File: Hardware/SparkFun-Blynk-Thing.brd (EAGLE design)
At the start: 50 x 41.9 mm, 103 parts, among them IC1 LMV358, Q1 2.5A/30V, Q2 MMBT2222A, Q3 MMBT2222A, U1 MCP73831, U2 ESP8266, U3 AP2112K-3.3V, U4 FT231XS-U, U5 W25Q32FVSS, U6 SI7021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

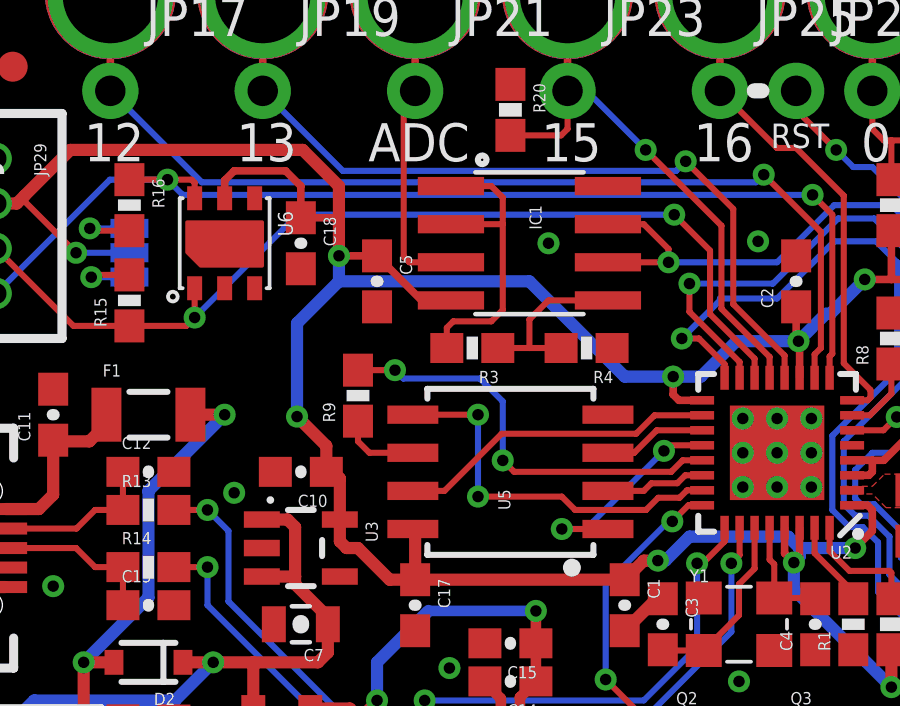
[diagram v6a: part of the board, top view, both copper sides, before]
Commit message: Fixing Op amp power supply.
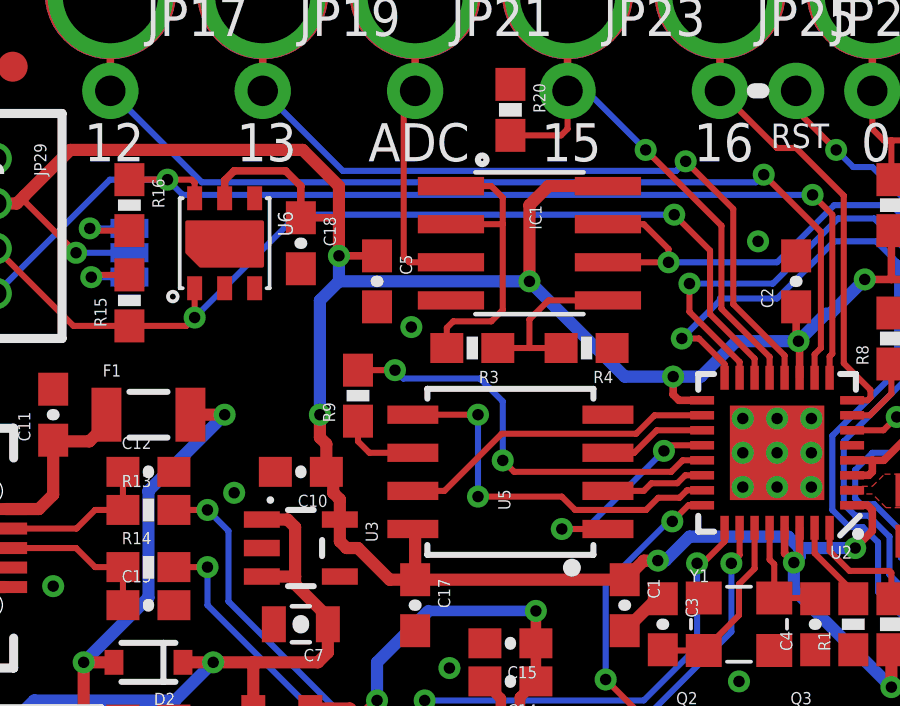
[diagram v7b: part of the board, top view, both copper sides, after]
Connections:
- net GND: now also IC1.4; no longer IC1.8
- net VCC: now also IC1.8; no longer IC1.4
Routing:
- net VCC: track 159.2 -> 160.8 mm, vias 11 -> 12
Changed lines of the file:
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@@
 <contactref element="D4" pad="1"/>
 <contactref element="C9" pad="1"/>
-<contactref element="IC1" pad="4"/>
 <contactref element="C5" pad="1"/>
 <contactref element="JP4" pad="1@2"/>
@@
 <wire x1="15.875" y1="31.965" x2="15.875" y2="30.695" width="0.4064" layer="1"/>
 <wire x1="15.875" y1="30.695" x2="15.875" y2="29.845" width="0.4064" layer="16"/>
-<wire x1="15.9051" y1="21.905" x2="15.9051" y2="23.2744" width="0.4064" layer="1"/>
-<wire x1="15.9051" y1="23.2744" x2="15.6845" y2="23.495" width="0.4064" layer="1"/>
 <wire x1="15.6845" y1="23.495" x2="15.455" y2="23.495" width="0.4064" layer="1"/>
-<wire x1="15.455" y1="23.495" x2="15.455" y2="24.3595" width="0.4064" layer="1"/>
-<wire x1="15.455" y1="24.3595" x2="14.478" y2="25.3365" width="0.4064" layer="1"/>
-<wire x1="14.478" y1="25.3365" x2="14.478" y2="28.448" width="0.4064" layer="16"/>
 <wire x1="14.605" y1="31.965" x2="15.875" y2="31.965" width="0.254" layer="1"/>
 <wire x1="14.605" y1="31.965" x2="14.605" y2="33.02" width="0.254" layer="1"/>
@@
 <wire x1="13.335" y1="2.54" x2="13.335" y2="5.715" width="0.254" layer="1"/>
 <wire x1="34.29" y1="16.3195" x2="35.1155" y2="16.3195" width="0.4064" layer="1"/>
-<via x="14.478" y="25.3365" extent="1-16" drill="0.381"/>
+<via x="15.24" y="25.4" extent="1-16" drill="0.381"/>
 <via x="15.875" y="30.695" extent="1-16" drill="0.381"/>
 <wire x1="15.875" y1="30.695" x2="17.145" y2="30.695" width="0.254" layer="1"/>
-<wire x1="17.145" y1="30.695" x2="18.63" y2="29.21" width="0.254" layer="1"/>
-<wire x1="18.63" y1="29.21" x2="19.6088" y2="29.21" width="0.254" layer="1"/>
-<wire x1="19.685" y1="29.21" x2="19.6088" y2="29.21" width="0.254" layer="1"/>
 <wire x1="32.98" y1="23.38" x2="33.54" y2="23.38" width="0.254" layer="1"/>
 <wire x1="33.54" y1="23.38" x2="33.655" y2="23.495" width="0.254" layer="1"/>
@@
 <wire x1="25.4" y1="26.67" x2="22.225" y2="29.845" width="0.4064" layer="16"/>
 <wire x1="22.225" y1="29.845" x2="15.875" y2="29.845" width="0.4064" layer="16"/>
-<wire x1="14.478" y1="28.448" x2="15.875" y2="29.845" width="0.4064" layer="16"/>
 <via x="33.401" y="29.9085" extent="1-16" drill="0.381"/>
 <wire x1="33.655" y1="22.225" x2="33.655" y2="21.5265" width="0.254" layer="1"/>
@@
 <wire x1="18.415" y1="21.5138" x2="18.415" y2="19.9" width="0.4064" layer="1"/>
 <wire x1="30.099" y1="7.239" x2="35.345" y2="12.485" width="0.4064" layer="16"/>
+<contactref element="IC1" pad="8"/>
+<via x="22.225" y="29.845" extent="1-16" drill="0.381"/>
+<wire x1="22.225" y1="29.845" x2="22.225" y2="32.385" width="0.4064" layer="1"/>
+<wire x1="22.225" y1="32.385" x2="22.86" y2="33.02" width="0.4064" layer="1"/>
+<wire x1="22.86" y1="33.02" x2="24.8412" y2="33.02" width="0.4064" layer="1"/>
+<wire x1="15.24" y1="25.4" x2="15.24" y2="24.638" width="0.4064" layer="1"/>
+<wire x1="15.24" y1="24.638" x2="15.455" y2="24.423" width="0.4064" layer="1"/>
+<wire x1="15.455" y1="24.423" x2="15.455" y2="23.495" width="0.4064" layer="1"/>
+<wire x1="15.6845" y1="23.495" x2="15.6845" y2="22.7965" width="0.4064" layer="1"/>
+<wire x1="15.6845" y1="22.7965" x2="15.9051" y2="22.5759" width="0.4064" layer="1"/>
+<wire x1="15.9051" y1="21.905" x2="15.9051" y2="22.5759" width="0.4064" layer="1"/>
+<wire x1="15.24" y1="25.4" x2="15.24" y2="29.21" width="0.4064" layer="16"/>
+<wire x1="15.24" y1="29.21" x2="15.875" y2="29.845" width="0.4064" layer="16"/>
 </signal>
 <signal name="GND">
@@
 <contactref element="C9" pad="2"/>
 <contactref element="R4" pad="1"/>
-<contactref element="IC1" pad="8"/>
 <contactref element="C5" pad="2"/>
 <polygon width="0.254" layer="1" isolate="0.2032" orphans="yes" rank="6">
@@
 <via x="29.845" y="31.1785" extent="1-16" drill="0.381"/>
 <via x="12.3825" y="22.7965" extent="1-16" drill="0.381"/>
-<via x="22.86" y="31.115" extent="1-16" drill="0.381"/>
+<via x="18.288" y="28.321" extent="1-16" drill="0.381"/>
 <via x="29.21" y="16.51" extent="1-16" drill="0.381"/>
 <via x="36.195" y="21.59" extent="1-16" drill="0.381"/>
@@
 <wire x1="26.67" y1="19.265" x2="26.465" y2="19.265" width="0.4064" layer="1"/>
 <wire x1="26.465" y1="19.265" x2="25.4" y2="18.2" width="0.4064" layer="1"/>
+<contactref element="IC1" pad="4"/>
 </signal>
 <signal name="N$1">
@@
 <contactref element="IC1" pad="2"/>
 <wire x1="19.47" y1="27.6225" x2="19.47" y2="28.2965" width="0.2032" layer="1"/>
-<wire x1="19.47" y1="28.2965" x2="19.685" y2="28.5115" width="0.2032" layer="1"/>
-<wire x1="19.685" y1="28.5115" x2="20.955" y2="28.5115" width="0.2032" layer="1"/>
-<wire x1="20.955" y1="28.5115" x2="21.336" y2="28.8925" width="0.2032" layer="1"/>
 <wire x1="21.336" y1="28.8925" x2="21.336" y2="31.75" width="0.2032" layer="1"/>
 <wire x1="21.336" y1="31.75" x2="21.336" y2="32.639" width="0.2032" layer="1"/>
@@
 <wire x1="20.955" y1="33.02" x2="19.6088" y2="33.02" width="0.2032" layer="1"/>
 <wire x1="19.6088" y1="31.75" x2="21.336" y2="31.75" width="0.2032" layer="1"/>
+<wire x1="19.47" y1="28.2965" x2="19.685" y2="28.5115" width="0.2032" layer="1"/>
+<wire x1="19.685" y1="28.5115" x2="20.955" y2="28.5115" width="0.2032" layer="1"/>
+<wire x1="20.955" y1="28.5115" x2="21.336" y2="28.8925" width="0.2032" layer="1"/>
 </signal>
 <signal name="N$18">
